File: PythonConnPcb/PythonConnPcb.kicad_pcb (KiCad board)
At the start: 2 copper layers, 17 x 45 mm, 9 parts, among them Q1 LED_5050, SW1 SS-12F23

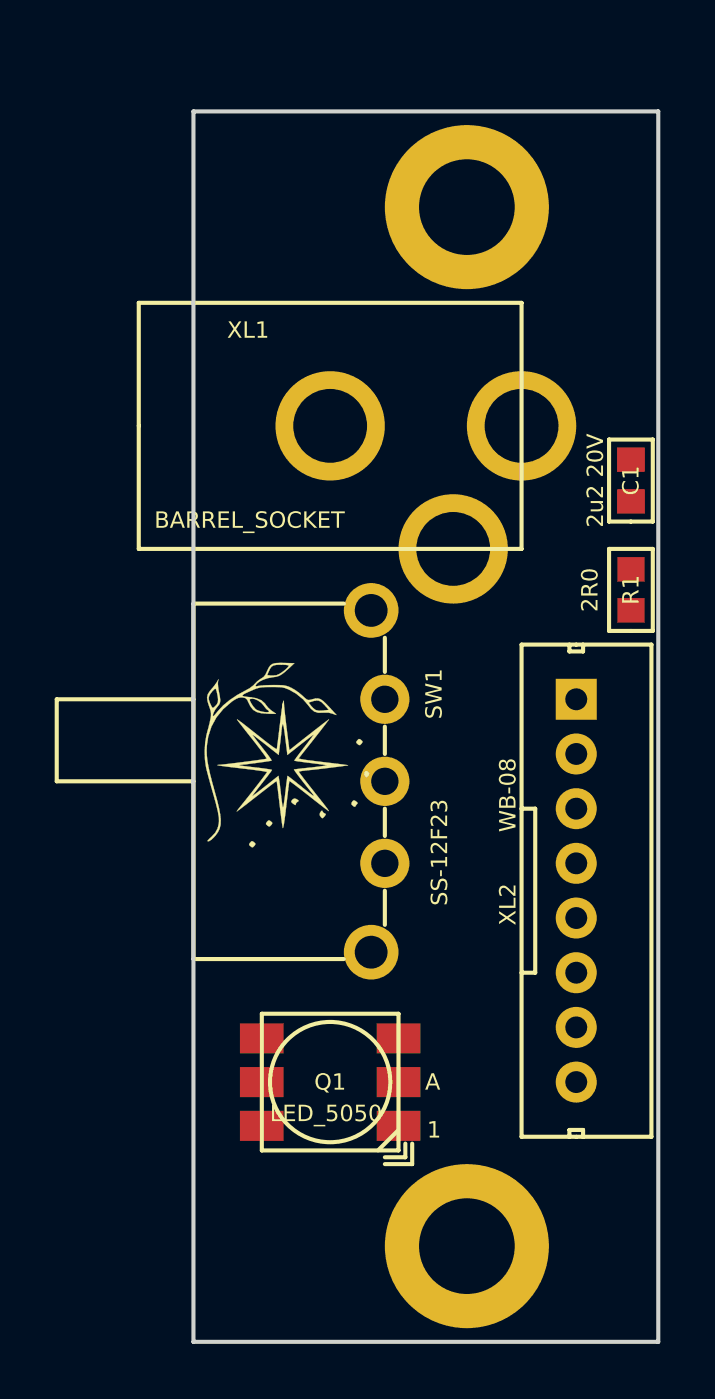
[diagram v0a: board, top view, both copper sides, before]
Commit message: V3 sent to factory
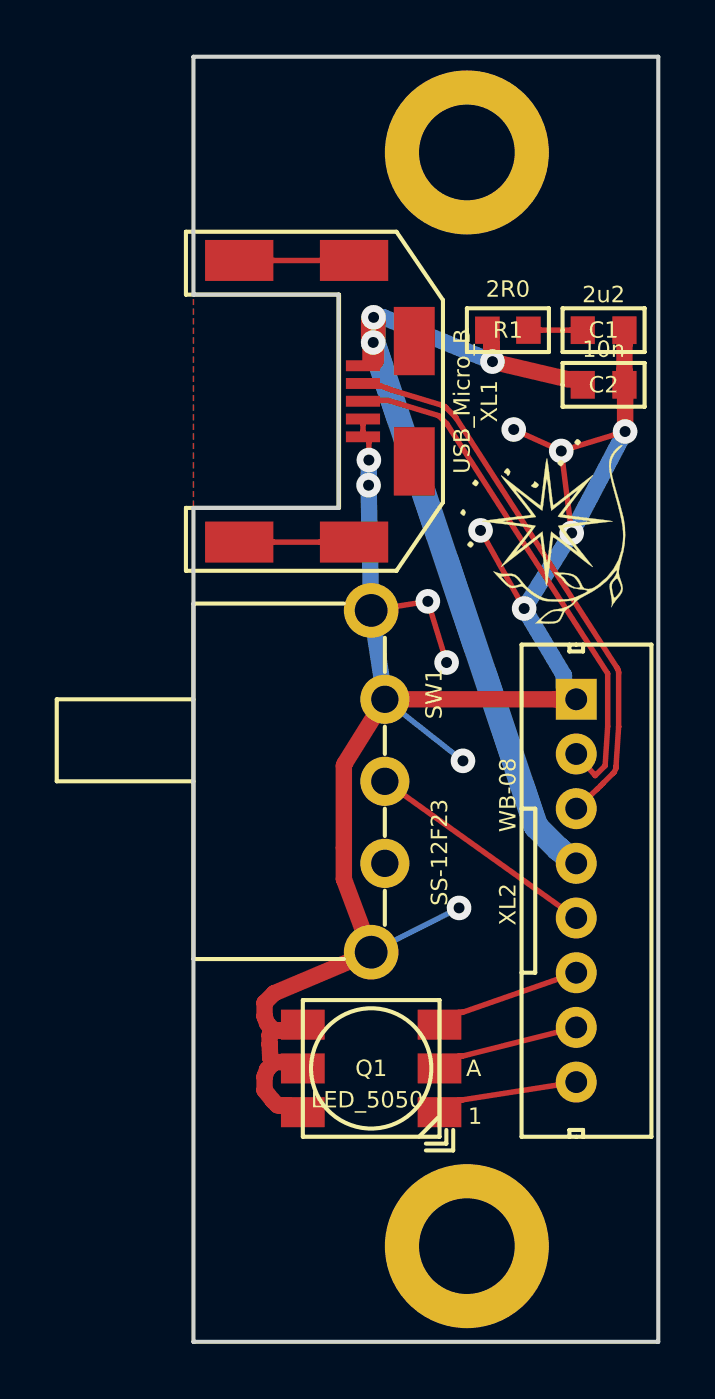
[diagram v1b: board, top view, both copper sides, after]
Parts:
- added C2: 10n, Capacitors:CAP_0603, F.Cu at (162.0, 50.5)
- C1: value 2u2 20V -> 2u2
- XL1: value BARREL_SOCKET -> USB_Micro_B; footprint Connectors:Barrel -> Connectors:USBmicro_MOLEX_WM17142
- moved Logo1 13.2 mm to (160.0, 55.5), turned to 90 degrees
- moved R1 10.5 mm to (158.5, 48.5), turned to 0 degrees
- moved XL1 6.74 mm to (152.3, 51.1)
- moved C1 5.59 mm to (162.0, 48.5), turned to 0 degrees
- moved HOLE1 2.00 mm to (157.0, 42.0)
- moved Q1 1.58 mm to (153.5, 75.5)
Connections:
- HOLE1 pad H: GNDPWR -> (no net)
- HOLE2 pad H: GNDPWR -> (no net)
- R1 pad 1: /PWR_EXT -> /5V
- XL2 pad 1: /PWR_EXT -> GNDPWR
- XL2 pad 2: /PWR_EXT -> /D+
- XL2 pad 3: /R -> /D-
- XL2 pad 4: /G -> /5V
- XL2 pad 5: /B -> /OnOff
- XL2 pad 6: /OnOff -> /R
- XL2 pad 7: GNDPWR -> /G
- XL2 pad 8: GNDPWR -> /B
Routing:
- net GNDPWR: track 0.00 -> 76.5 mm, vias 0 -> 12
- net /5V: track 0.00 -> 33.0 mm, vias 0 -> 3
- net /D-: track 0.00 -> 20.3 mm
- net /D+: track 0.00 -> 19.1 mm
- net /OnOff: track 0.00 -> 8.60 mm
- net /R: track 0.00 -> 5.38 mm
- net /G: track 0.00 -> 5.26 mm
- net /B: track 0.00 -> 5.18 mm
- net Net-(XL1-PadH4): track 0.00 -> 4.20 mm
- net Net-(XL1-PadH1): track 0.00 -> 4.20 mm
- net Net-(C1-Pad1): track 0.00 -> 1.99 mm
- added copper zone on B.Cu, net GNDPWR
- added copper zone on F.Cu, net GNDPWR
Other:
- board size 17 x 45 mm -> 17 x 47 mm
- net class Default: trace_width 0.25 -> 0.2; via_dia 0.8 -> 0.9
- rule pad_to_mask_clearance: 0.2 -> 0.1
